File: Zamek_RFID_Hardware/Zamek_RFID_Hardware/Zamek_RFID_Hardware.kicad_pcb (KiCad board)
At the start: 2 copper layers, 43.2 x 17.8 mm, 6 parts, among them J1 Analog, J2 Digital

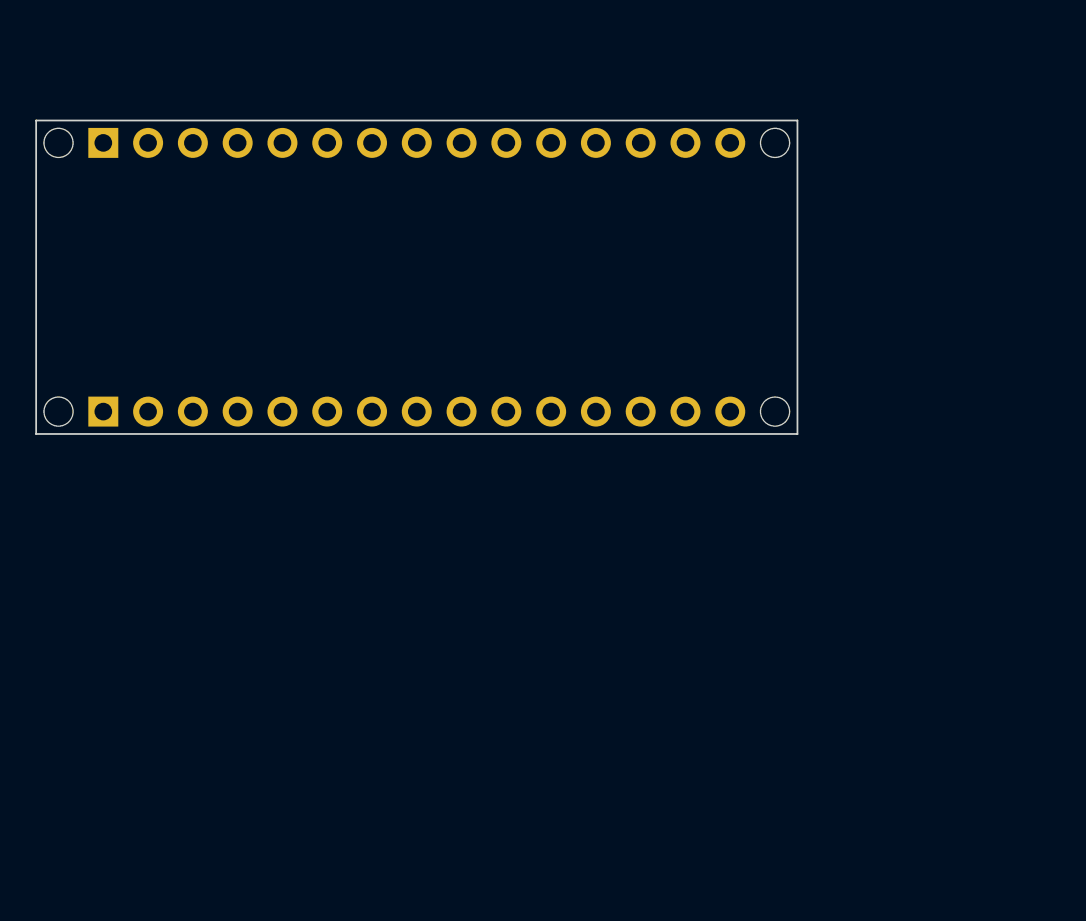
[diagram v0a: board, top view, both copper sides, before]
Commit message: Projekt PCB: Ułożenie elementów i narysowanie krawędzi płytki (Widok 3D)
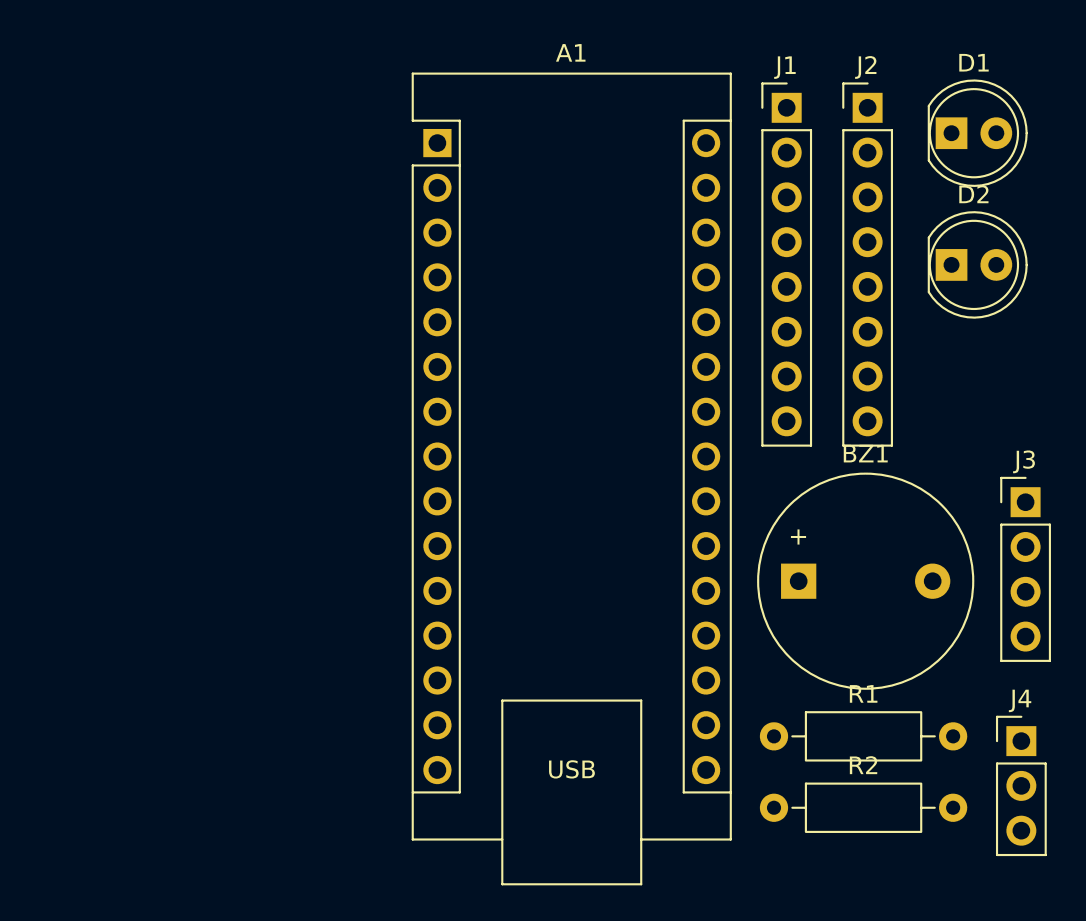
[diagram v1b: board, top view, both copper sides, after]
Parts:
- removed MH1, MH2, MH3, MH4: MountingHole_65mil, Arduino_MountingHole:MountingHole_65mil
- added A1: Arduino_Nano_v3.x, Module:Arduino_Nano, F.Cu at (122.8, 83.5)
- added BZ1: Buzzer, Buzzer_Beeper:Buzzer_12x9.5RM7.6, F.Cu at (143.2, 108.3)
- added D1: LED, LED_THT:LED_D5.0mm, F.Cu at (151.9, 82.9)
- added D2: LED, LED_THT:LED_D5.0mm, F.Cu at (151.9, 90.4)
- added J3: Conn_01x04, Connector_PinHeader_2.54mm:PinHeader_1x04_P2.54mm_Vertical, F.Cu at (156.1, 103.9)
- added J4: Conn_01x03, Connector_PinHeader_2.54mm:PinHeader_1x03_P2.54mm_Vertical, F.Cu at (155.9, 117.4)
- added R1: R, Resistor_THT:R_Axial_DIN0207_L6.3mm_D2.5mm_P10.16mm_Horizontal, F.Cu at (141.8, 117.2)
- added R2: R, Resistor_THT:R_Axial_DIN0207_L6.3mm_D2.5mm_P10.16mm_Horizontal, F.Cu at (141.8, 121.2)
- J1: value Analog -> Conn_01x08; footprint Connector_PinHeader_2.54mm:PinHeader_1x15_P2.54mm_Vertical -> Connector_PinHeader_2.54mm:PinHeader_1x08_P2.54mm_Vertical; moved to F.Cu
- J2: value Digital -> Conn_01x08; footprint Connector_PinHeader_2.54mm:PinHeader_1x15_P2.54mm_Vertical -> Connector_PinHeader_2.54mm:PinHeader_1x08_P2.54mm_Vertical; moved to F.Cu
- moved J2 43.4 mm to (147.2, 81.5), turned to 0 degrees
- moved J1 42.4 mm to (142.6, 81.5), turned to 0 degrees
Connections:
- J1 pad 1: /D13/SCK -> +3.3V
- J1 pad 2: +3V3 -> +3.3V
- J1 pad 3: /AREF -> +3.3V
- J1 pad 4: /A0 -> unconnected-(J1-Pin_4-Pad4)
- J1 pad 5: /A1 -> /RFID_MISO
- J1 pad 6: /A2 -> /RFID_MOSI
- J1 pad 7: /A3 -> /RFID_SCK
- J1 pad 8: /A4/SDA -> /RFID_SDA
- J2 pad 1: /D12/MISO -> /KEY_C4
- J2 pad 2: /*D11/MOSI -> /KEY_C3
- J2 pad 3: /*D10/SS -> /KEY_C2
- J2 pad 4: /*D9 -> /KEY_C1
- J2 pad 5: /D8 -> /KEY_R1
- J2 pad 6: /D7 -> /KEY_R2
- J2 pad 7: /*D6 -> /KEY_R3
- J2 pad 8: /*D5 -> /KEY_R4
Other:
- board outline removed
- board text removed: "ICSP"
- board text removed: "USB Mini-B"

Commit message: poprawki i wylewka
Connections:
- A1 pad 29: unconnected-(A1-GND-Pad29) -> GND
- A1 pad 4: +3.3V -> GND
- BZ1 pad 2: +3.3V -> GND
- D1 pad 2: +3.3V -> GND
- D2 pad 2: +3.3V -> GND
- J1 pad 3: +3.3V -> GND
- J3 pad 1: +3.3V -> GND
- J4 pad 2: +3.3V -> GND
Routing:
- net GND: track 0.00 -> 261.8 mm
- net /KEY_C2: track 0.00 -> 118.2 mm
- net /KEY_C1: track 0.00 -> 112.6 mm
- net /KEY_R1: track 0.00 -> 109.2 mm
- net /KEY_R2: track 0.00 -> 105.3 mm
- net /KEY_R3: track 0.00 -> 102.3 mm
- net /KEY_R4: track 0.00 -> 99.7 mm
- net /RFID_MISO: track 0.00 -> 76.7 mm
- net /RFID_SDA: track 0.00 -> 76.3 mm
- net /RFID_MOSI: track 0.00 -> 75.2 mm
- net +5V: track 0.00 -> 65.5 mm
- net /PRZEKAŹNIK: track 0.00 -> 60.8 mm
- net /I2C_SCL: track 0.00 -> 54.1 mm
- net /KEY_C4: track 0.00 -> 53.4 mm, vias 0 -> 1
- net /I2C_SDA: track 0.00 -> 52.6 mm
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- added copper zone on B.Cu, net GND

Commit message: poprawki
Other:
- board outline added: 53.6 x 61.5 mm

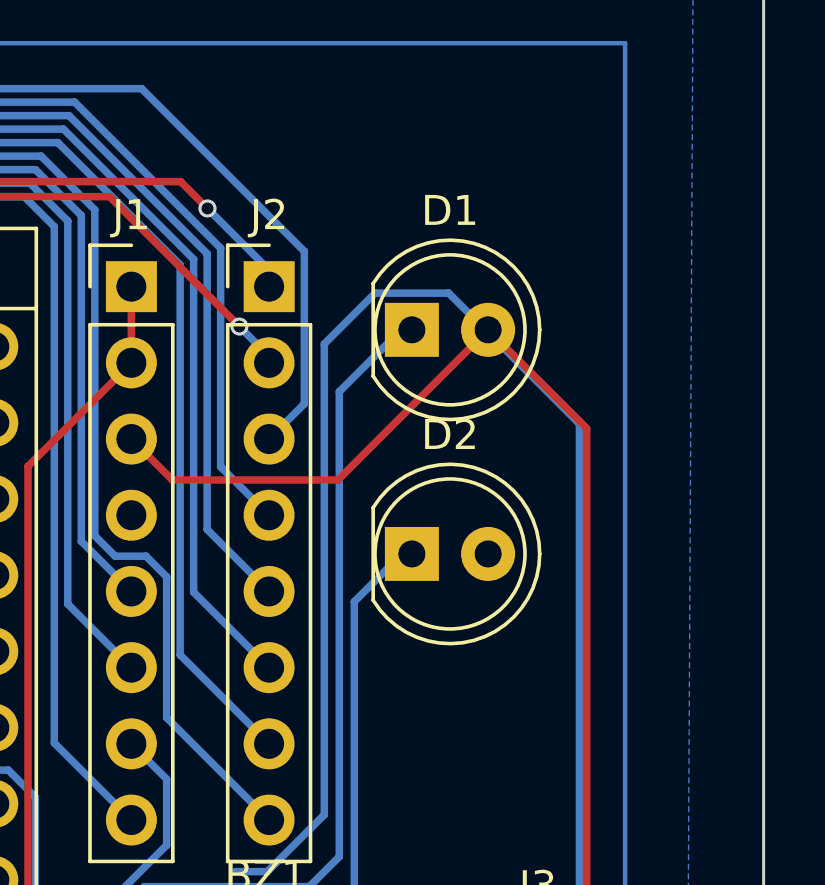
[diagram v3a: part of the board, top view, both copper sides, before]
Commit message: hw: schematic v1.1 - fix LED polarity, add decoupling, SPI level shifting and buzzer driver
- Rotate D1/D2 so the GPIO drives the anode through the resistor;
  PCB footprints rotated 180 deg in place, existing copper reused
- R1 = 300 R, R2 = 200 R (10 mA per LED)
- Add 100 uF + 100 nF on +5V at the relay connector and
  10 uF + 100 nF on +3.3V at the RC522 connector
- Add 1k/2k dividers on SS, MOSI and SCK: MFRC522 inputs are limited
  to VDD + 0.5 V; MISO stays direct (3.3 V is above ATmega328P VIH)
- Drive the buzzer through a BC547 with a 1N4148 flyback diode
- Add test points on +5V, +3.3V and GND, and four M3 mounting holes
- Rename net PRZEKAZNIK to RELAY (ASCII only for CAM tools)
- ERC clean: no-connect flags on unused Nano pins, PWR_FLAG on GND

PCB layout not yet updated from the schematic.
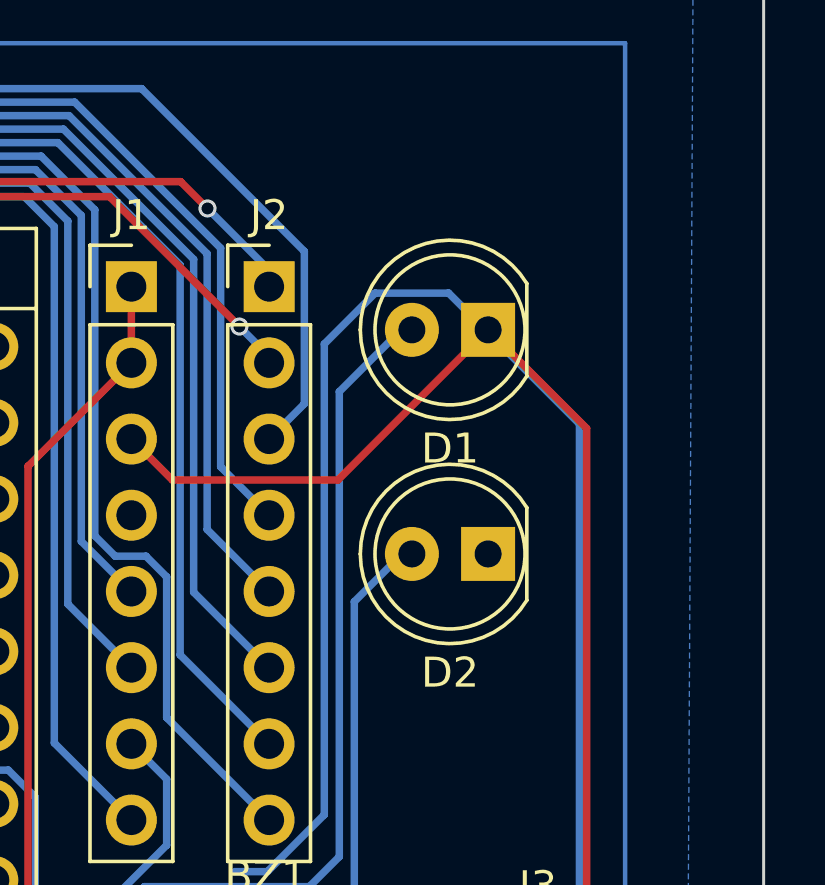
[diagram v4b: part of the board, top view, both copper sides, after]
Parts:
- moved D1 2.54 mm to (154.5, 82.9), turned to 180 degrees
- moved D2 2.54 mm to (154.5, 90.4), turned to 180 degrees
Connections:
- D1 pad 1: Net-(D1-K) -> GND
- D1 pad 2: GND -> Net-(D1-A)
- D2 pad 1: Net-(D2-K) -> GND
- D2 pad 2: GND -> Net-(D2-A)
- R1 pad 1: Net-(D1-K) -> Net-(D1-A)
- R2 pad 1: Net-(D2-K) -> Net-(D2-A)
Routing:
- net Net-(D2-K): track 50.1 -> 0.00 mm
- net Net-(D2-A): track 0.00 -> 50.1 mm
- net Net-(D1-K): track 43.3 -> 0.00 mm
- net Net-(D1-A): track 0.00 -> 43.3 mm
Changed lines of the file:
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@@
 	(footprint "LED_THT:LED_D5.0mm"
 		(layer "F.Cu")
-		(at 151.92 82.94)
+		(at 154.46 82.94 180)
 		(descr "LED, diameter 5.0mm, 2 pins, http://cdn-reichelt.de/documents/datenblatt/A500/LL-504BC2E-009.pdf, generated by kicad-footprint-generator")
 		(tags "LED")
@@
 		)
 		(property "Sim.Pins" "1=K 2=A"
-			(at 0 0 0)
+			(at 0 0 180)
 			(unlocked yes)
 			(layer "F.Fab")
@@
 		)
 		(fp_arc
-			(start -1.29 -1.54483)
-			(mid 2.071779 -2.880495)
-			(end 4.26 0)
+			(start 4.26 0)
+			(mid 2.071779 2.880495)
+			(end -1.29 1.54483)
 			(stroke
 				(width 0.12)
@@
 		)
 		(fp_arc
-			(start 4.26 0)
-			(mid 2.071779 2.880495)
-			(end -1.29 1.54483)
+			(start -1.29 -1.54483)
+			(mid 2.071779 -2.880495)
+			(end 4.26 0)
 			(stroke
 				(width 0.12)
@@
 		)
 		(pad "1" thru_hole rect
-			(at 0 0)
+			(at 0 0 180)
 			(size 1.8 1.8)
 			(drill 0.9)
 			(layers "*.Cu" "*.Mask")
 			(remove_unused_layers no)
-			(net "Net-(D1-K)")
+			(net "GND")
 			(pinfunction "K_1")
 			(pintype "passive")
 		)
 		(pad "2" thru_hole circle
-			(at 2.54 0)
+			(at 2.54 0 180)
 			(size 1.8 1.8)
 			(drill 0.9)
 			(layers "*.Cu" "*.Mask")
 			(remove_unused_layers no)
-			(net "GND")
+			(net "Net-(D1-A)")
 			(pinfunction "A_2")
 			(pintype "passive")
@@
 			(layers "*.Cu" "*.Mask")
 			(remove_unused_layers no)
-			(net "Net-(D1-K)")
+			(net "Net-(D1-A)")
 			(pintype "passive")
 		)
@@
 			(layers "*.Cu" "*.Mask")
 			(remove_unused_layers no)
-			(net "Net-(D2-K)")
+			(net "Net-(D2-A)")
 			(pintype "passive")
 		)
@@
 	(footprint "LED_THT:LED_D5.0mm"
 		(layer "F.Cu")
-		(at 151.92 90.41)
+		(at 154.46 90.41 180)
 		(descr "LED, diameter 5.0mm, 2 pins, http://cdn-reichelt.de/documents/datenblatt/A500/LL-504BC2E-009.pdf, generated by kicad-footprint-generator")
 		(tags "LED")
@@
 		)
 		(property "Sim.Pins" "1=K 2=A"
-			(at 0 0 0)
+			(at 0 0 180)
 			(unlocked yes)
 			(layer "F.Fab")
@@
 		)
 		(fp_arc
-			(start -1.29 -1.54483)
-			(mid 2.071779 -2.880495)
-			(end 4.26 0)
+			(start 4.26 0)
+			(mid 2.071779 2.880495)
+			(end -1.29 1.54483)
 			(stroke
 				(width 0.12)
@@
 		)
 		(fp_arc
-			(start 4.26 0)
-			(mid 2.071779 2.880495)
-			(end -1.29 1.54483)
+			(start -1.29 -1.54483)
+			(mid 2.071779 -2.880495)
+			(end 4.26 0)
 			(stroke
 				(width 0.12)
@@
 		)
 		(pad "1" thru_hole rect
-			(at 0 0)
+			(at 0 0 180)
 			(size 1.8 1.8)
 			(drill 0.9)
 			(layers "*.Cu" "*.Mask")
 			(remove_unused_layers no)
-			(net "Net-(D2-K)")
+			(net "GND")
 			(pinfunction "K_1")
 			(pintype "passive")
 		)
 		(pad "2" thru_hole circle
-			(at 2.54 0)
+			(at 2.54 0 180)
 			(size 1.8 1.8)
 			(drill 0.9)
 			(layers "*.Cu" "*.Mask")
 			(remove_unused_layers no)
-			(net "GND")
+			(net "Net-(D2-A)")
 			(pinfunction "A_2")
 			(pintype "passive")
@@
 		(width 0.25)
 		(layer "B.Cu")
-		(net "Net-(D1-K)")
+		(net "Net-(D1-A)")
 	)
 	(segment
@@
 		(width 0.25)
 		(layer "B.Cu")
-		(net "Net-(D1-K)")
+		(net "Net-(D1-A)")
 	)
 	(segment
@@
 		(width 0.25)
 		(layer "B.Cu")
-		(net "Net-(D1-K)")
+		(net "Net-(D1-A)")
 	)
 	(segment
@@
 		(width 0.25)
 		(layer "B.Cu")
-		(net "Net-(D1-K)")
+		(net "Net-(D1-A)")
 	)
 	(segment
@@
 		(width 0.25)
 		(layer "B.Cu")
-		(net "Net-(D1-K)")
+		(net "Net-(D1-A)")
 	)
 	(segment
@@
 		(width 0.25)
 		(layer "B.Cu")
-		(net "Net-(D1-K)")
+		(net "Net-(D1-A)")
 	)
 	(segment
@@
 		(width 0.25)
 		(layer "B.Cu")
-		(net "Net-(D1-K)")
+		(net "Net-(D1-A)")
 	)
 	(segment
@@
 		(width 0.25)
 		(layer "B.Cu")
-		(net "Net-(D1-K)")
+		(net "Net-(D1-A)")
 	)
 	(segment
@@
 		(width 0.25)
 		(layer "B.Cu")
-		(net "Net-(D2-K)")
+		(net "Net-(D2-A)")
 	)
 	(segment
@@
 		(width 0.25)
 		(layer "B.Cu")
-		(net "Net-(D2-K)")
+		(net "Net-(D2-A)")
 	)
 	(segment
@@
 		(width 0.25)
 		(layer "B.Cu")
-		(net "Net-(D2-K)")
+		(net "Net-(D2-A)")
 	)
 	(segment
@@
 		(width 0.25)
 		(layer "B.Cu")
-		(net "Net-(D2-K)")
+		(net "Net-(D2-A)")
 	)
 	(segment
@@
 		(width 0.25)
 		(layer "B.Cu")
-		(net "Net-(D2-K)")
+		(net "Net-(D2-A)")
 	)
 	(segment
@@
 		(width 0.25)
 		(layer "B.Cu")
-		(net "Net-(D2-K)")
+		(net "Net-(D2-A)")
 	)
 	(segment
@@
 		(width 0.25)
 		(layer "B.Cu")
-		(net "Net-(D2-K)")
+		(net "Net-(D2-A)")
 	)
 	(segment
@@
 		(width 0.25)
 		(layer "B.Cu")
-		(net "Net-(D2-K)")
+		(net "Net-(D2-A)")
 	)
 	(segment
@@
 		(width 0.25)
 		(layer "B.Cu")
-		(net "Net-(D2-K)")
+		(net "Net-(D2-A)")
 	)
 	(segment

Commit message: after F8 and cleaning
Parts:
- added C1: 100uF 16V, Capacitor_THT:CP_Radial_D6.3mm_P2.50mm, F.Cu at (158.6, 151.0)
- added C2: 100nF, Capacitor_THT:C_Disc_D5.0mm_W2.5mm_P5.00mm, F.Cu at (157.3, 141.0)
- added C3: 10uF 16V, Capacitor_THT:CP_Radial_D5.0mm_P2.00mm, F.Cu at (162.2, 158.2)
- added C4: 100nF, Capacitor_THT:C_Disc_D5.0mm_W2.5mm_P5.00mm, F.Cu at (157.3, 145.1)
- added D3: 1N4148, Diode_THT:D_DO-35_SOD27_P7.62mm_Horizontal, F.Cu at (136.1, 169.1)
- added H1: MountingHole, MountingHole:MountingHole_3.2mm_M3, F.Cu at (151.8, 143.0)
- added H2: MountingHole, MountingHole:MountingHole_3.2mm_M3, F.Cu at (151.8, 150.9)
- added H3: MountingHole, MountingHole:MountingHole_3.2mm_M3, F.Cu at (151.8, 158.9)
- added H4: MountingHole, MountingHole:MountingHole_3.2mm_M3, F.Cu at (151.8, 166.8)
- added Q1: BC547, Package_TO_SOT_THT:TO-92_Inline, F.Cu at (161.8, 164.8)
- added R3: 1k, Resistor_THT:R_Axial_DIN0207_L6.3mm_D2.5mm_P10.16mm_Horizontal, F.Cu at (136.1, 141.0)
- added R4: 1k, Resistor_THT:R_Axial_DIN0207_L6.3mm_D2.5mm_P10.16mm_Horizontal, F.Cu at (136.1, 145.1)
- added R5: 2k, Resistor_THT:R_Axial_DIN0207_L6.3mm_D2.5mm_P10.16mm_Horizontal, F.Cu at (136.1, 149.1)
- added R6: 2K, Resistor_THT:R_Axial_DIN0207_L6.3mm_D2.5mm_P10.16mm_Horizontal, F.Cu at (136.1, 153.2)
- added R7: 1k, Resistor_THT:R_Axial_DIN0207_L6.3mm_D2.5mm_P10.16mm_Horizontal, F.Cu at (136.1, 157.2)
- added R8: 2k, Resistor_THT:R_Axial_DIN0207_L6.3mm_D2.5mm_P10.16mm_Horizontal, F.Cu at (136.1, 161.3)
- added R9: 1k, Resistor_THT:R_Axial_DIN0207_L6.3mm_D2.5mm_P10.16mm_Horizontal, F.Cu at (136.1, 165.3)
- added TP1: TestPoint, TestPoint:TestPoint_THTPad_D2.0mm_Drill1.0mm, F.Cu at (157.8, 157.0)
- added TP2: TestPoint, TestPoint:TestPoint_THTPad_D2.0mm_Drill1.0mm, F.Cu at (157.8, 161.0)
- added TP3: TestPoint, TestPoint:TestPoint_THTPad_D2.0mm_Drill1.0mm, F.Cu at (157.8, 165.1)
- D1: value LED -> LED red 5mm
- D2: value LED -> LED green 5mm
- R1: value R -> 300
- R2: value R -> 200
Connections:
- net /PRZEKAŹNIK renamed /RELAY
- BZ1 pad 1: /BUZZER -> +5V
- BZ1 pad 2: GND -> Net-(BZ1--)
- J1 pad 6: /RFID_MOSI -> /RFID_MOSI_3V3
- J1 pad 7: /RFID_SCK -> /RFID_SCK_3V3
- J1 pad 8: /RFID_SDA -> /RFID_SDA_3V3
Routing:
- net /RFID_MISO: track 76.7 -> 0.00 mm
- net /RFID_SDA: track 76.3 -> 0.00 mm
- net /RFID_MOSI: track 75.2 -> 0.00 mm
- net /RFID_SCK: track 25.2 -> 0.00 mm
- net GND: track 261.8 -> 241.8 mm
- net /BUZZER: track 14.0 -> 0.00 mm, vias 1 -> 0
